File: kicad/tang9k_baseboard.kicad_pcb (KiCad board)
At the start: 2 copper layers, 99.1 x 81.3 mm, 47 parts, among them J1 FPGA I/O, J2 FPGA I/O, J3 PMOD-FULL, J4 PMOD-FULL, J5 PMOD-FULL, J6 PMOD-HALF, J7 SERLED OUT, J8 FPGA I/O, J9 FPGA I/O, U1 SN74LV1T34DBV, U2 AP2205-18W5-7

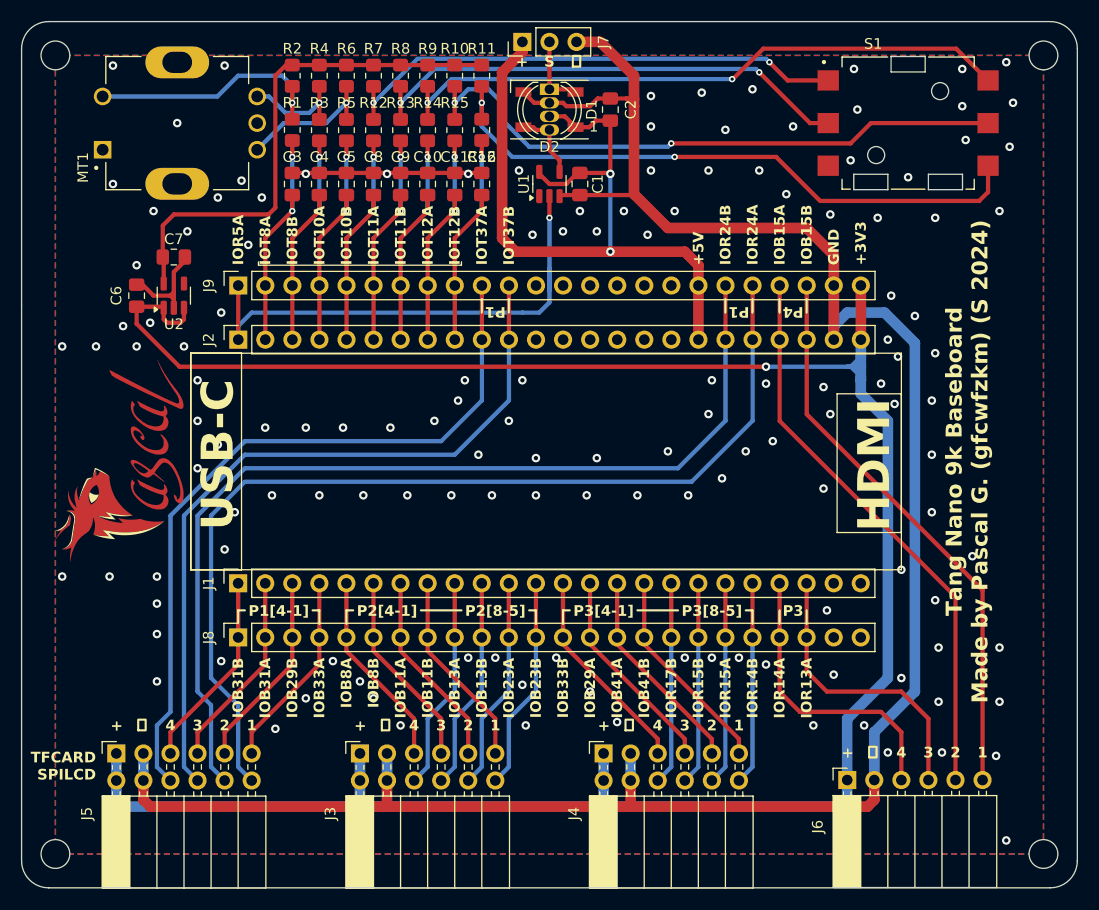
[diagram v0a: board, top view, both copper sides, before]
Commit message: Fixed minor silkscreen issues
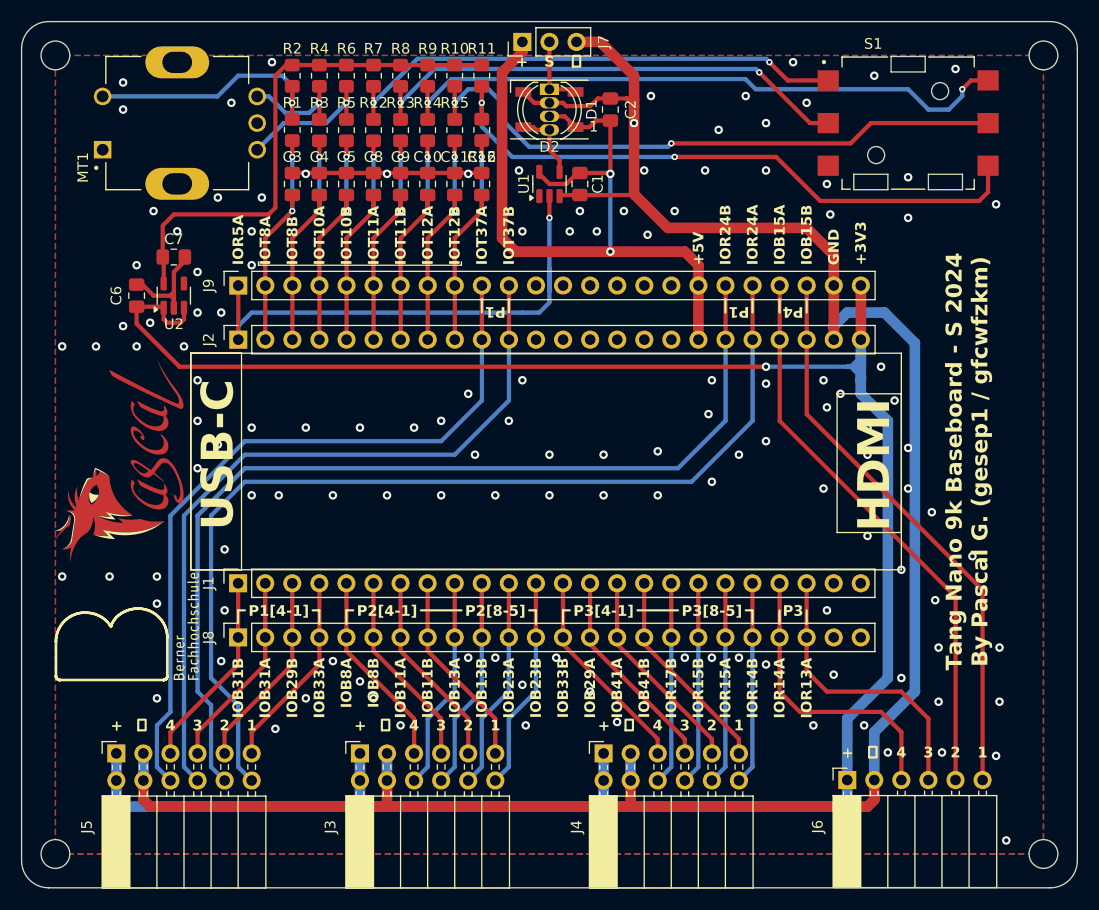
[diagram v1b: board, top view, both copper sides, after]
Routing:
- net GND: vias 141 -> 132
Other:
- board text added: "(Active-Low)"
- board text added: ": FPGA I/O :"
- board text added: "Board / PMOD I/O"
- board text added: "Center IOT10B"
- board text added: "CenterButton:IOT8A"
- board text added: "Down IOT12B"
- board text added: "IOB11A:P2.2"
- board text added: "IOB11B:P2.1"
- board text added: "IOB13A:P2.8"
- board text added: "IOB13B:P2.7"
- board text added: "IOB23A:P2.6"
- board text added: "IOB23B:P2.5"
- board text added: "IOB29A:P3.3"
- board text added: "IOB29B:P1.2"
- board text added: "IOB31A:P1.3"
- board text added: "IOB31B:P1.4"
- board text added: "IOB33A:P1.1"
- board text added: "IOB33B:P3.4"
- board text added: "IOB41A:P3.2"
- board text added: "IOB41B:P3.1"
- board text added: "IOB8A:P2.4"
- board text added: "IOB8B:P2.3"
- board text added: "IOR13A:P4.3"
- board text added: "IOR14A:P4.4"
- board text added: "IOR14B:P3.5"
- board text added: "IOR15A:P3.6"
- board text added: "IOR15B:P3.7"
- board text added: "IOR17B:P3.8"
- board text added: "JOYC:IOT10B"
- board text added: "JOYD:IOT12B"
- board text added: "JOYL:IOT11A"
- board text added: "JOYR:IOT12A"
- board text added: "JOYU:IOT11B"
- board text added: "Left IOT11A"
- board text added: "Navigation Joystick"
- board text added: "P1.5:IOR24A"
- board text added: "P1.6:IOR24B"
- board text added: "P1.7:IOT37B"
- board text added: "P1.8:IOT37A"
- board text added: "P4.1:IOB15B"
- board text added: "P4.2:IOB15A"
- board text added: "RGBL:IOR5A"
- board text added: "ROTA:IOT10A"
- board text added: "ROTB:IOT8B"
- board text added: "ROTC:IOT8A"
- board text added: "Right IOT12A"
- board text added: "Rotary Encoder"
- board text added: "RotaryA:IOT10A"
- board text added: "RotaryB:IOT8B"
- board text added: "Serial RGBLED Output Header"
- board text added: "Tang Nano 9k Baseboard - S 2024 By Pascal G. (gesep1 / gfcwfzkm)"
- board text added: "Up IOT11B"
- board text added: "WS2013-Style Serial RGBLED"
- board text removed: "Tang Nano 9k Baseboard Made by Pascal G. (gfcwfzkm) (S 2024)"

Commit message: Updated silkscreen & 3D renders
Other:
- board text added: "1.8V I/Os!"
- board text added: "25"
- board text added: "26"
- board text added: "27"
- board text added: "28"
- board text added: "29"
- board text added: "30"
- board text added: "31"
- board text added: "32"
- board text added: "33"
- board text added: "34"
- board text added: "35"
- board text added: "36"
- board text added: "37"
- board text added: "38"
- board text added: "39"
- board text added: "40"
- board text added: "41"
- board text added: "48"
- board text added: "49"
- board text added: "51"
- board text added: "52"
- board text added: "53"
- board text added: "54"
- board text added: "55"
- board text added: "56"
- board text added: "57"
- board text added: "63"
- board text added: "76"
- board text added: "77"
- board text added: "79"
- board text added: "80"
- board text added: "81"
- board text added: "82"
- board text added: "83"
- board text added: "84"
- board text added: "85"
- board text added: "86"
- board text added: "Feature PMOD"
- board text added: "PIN"
- board text added: "PMOD 1"
- board text added: "PMOD 2"
- board text added: "PMOD 3"
- board text added: "PMOD 4"
- board text removed: "Board / PMOD I/O"
